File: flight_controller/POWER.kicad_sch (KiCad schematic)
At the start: 3 parts, among them J10 A2012WV-S-9P

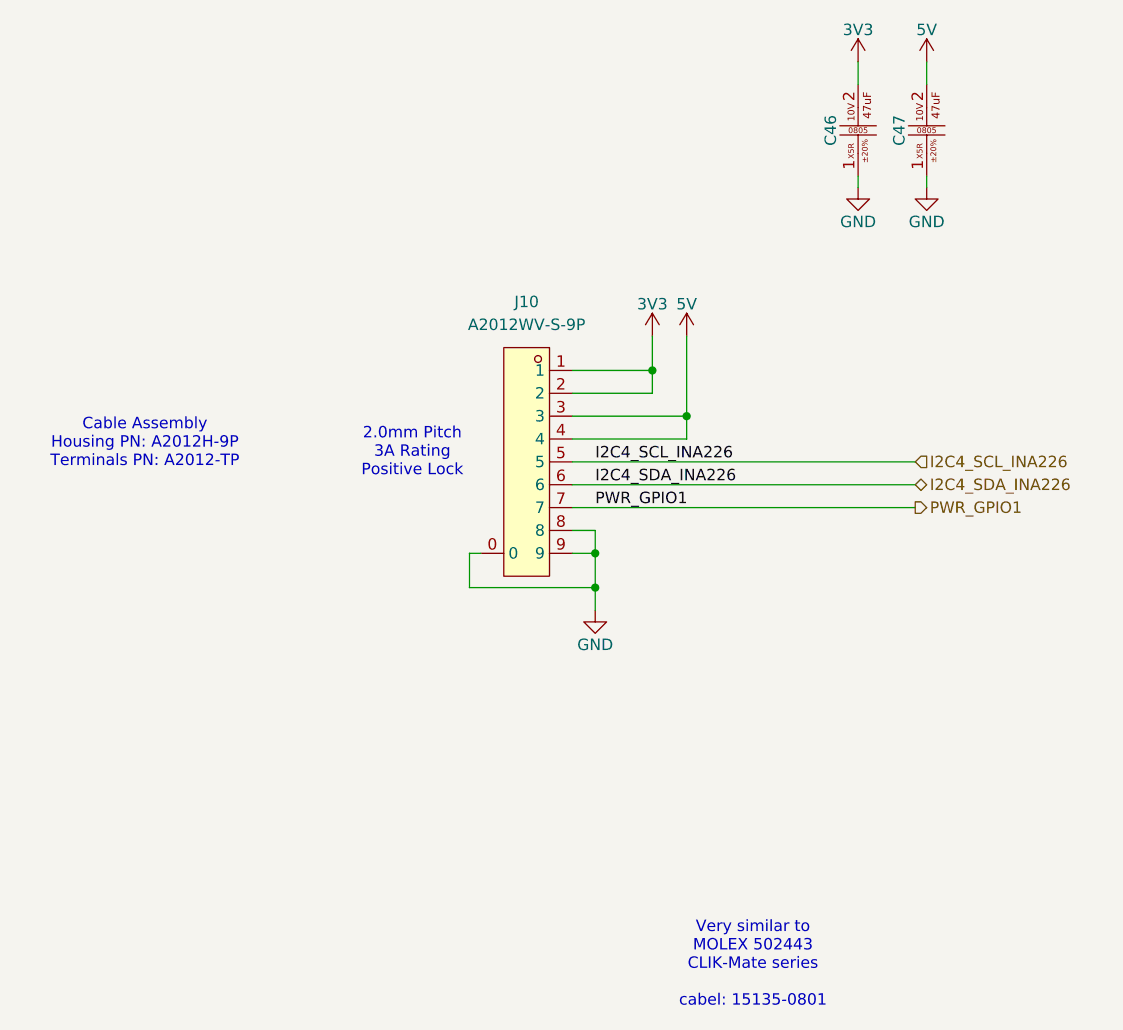
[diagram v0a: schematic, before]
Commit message: renamed some connectors to j instead of cn
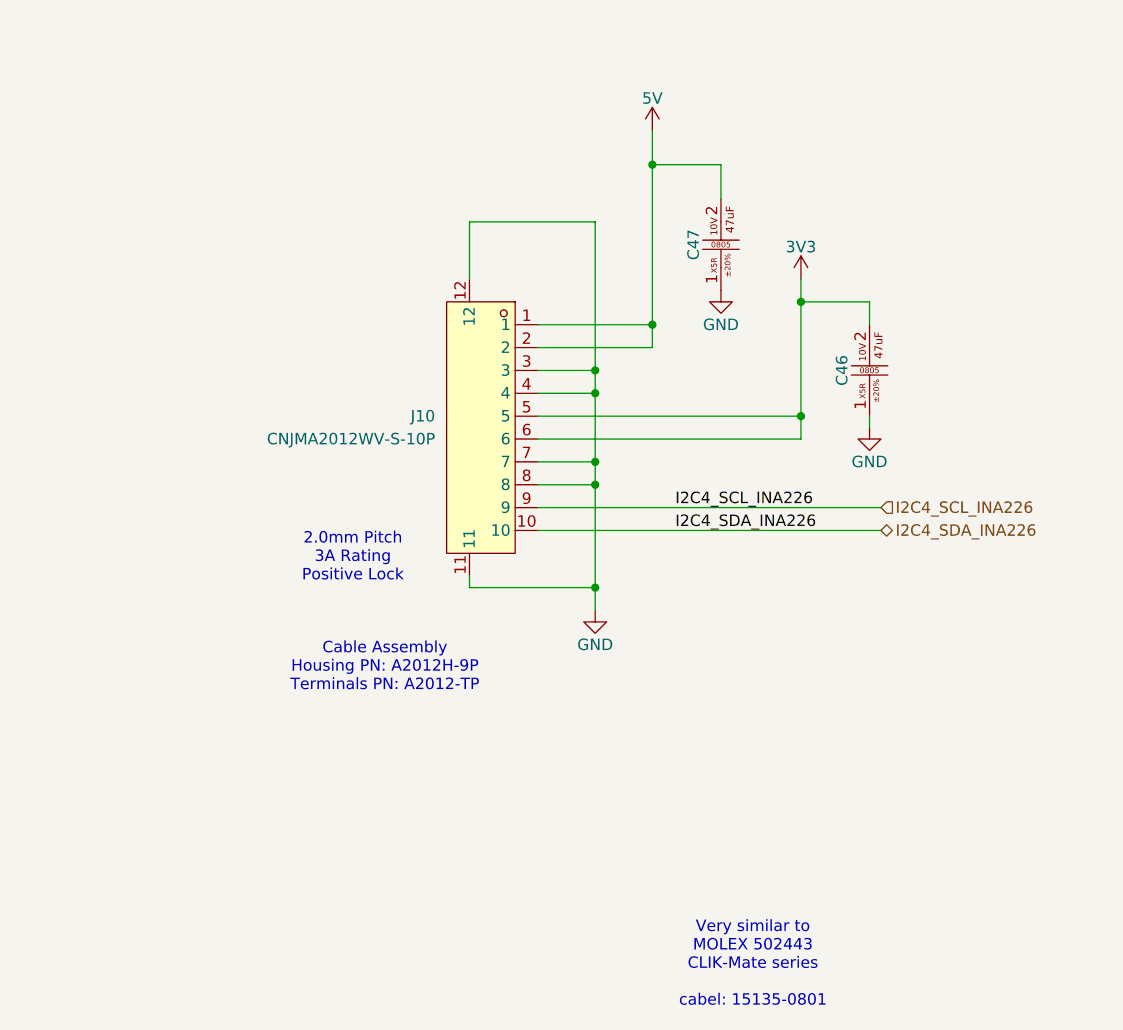
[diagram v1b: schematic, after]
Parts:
- removed J10: A2012WV-S-9P, easyeda2kicad:CONN-SMD_A2012WV-S-9P, symbol lampelKicadLIB:A2012WV-S-9P
- added J10: CNJMA2012WV-S-10P, easyeda2kicad:CONN-SMD_10P-P2.00_CNJM_CNJMA2012WV-S-10P, symbol easyeda_lampel:CNJMA2012WV-S-10P
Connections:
- net 3V3: now also J10.5, J10.6
- net 5V: now also J10.1, J10.2
- net GND: now also J10.11, J10.12, J10.3, J10.4, J10.7, J10.8
- net I2C4_SCL_INA226: now also J10.9
- net I2C4_SDA_INA226: now also J10.10
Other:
- moved on the sheet: C46, C47

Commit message: Advanced in routing
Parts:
- added C78, C81: GRM21BR61A476ME15L (47uF , 0805 ,10V ,X5R), easyeda2kicad:C0805, symbol lampelKicadLIB:GRM21BR61A476ME15L (47uF , 0805 ,10V ,X5R)
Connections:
- net 3V3: now also C78.2
- net 5V: now also C81.2
- net GND: now also C78.1, C81.1
